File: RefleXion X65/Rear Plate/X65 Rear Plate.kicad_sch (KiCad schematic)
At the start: 4 parts

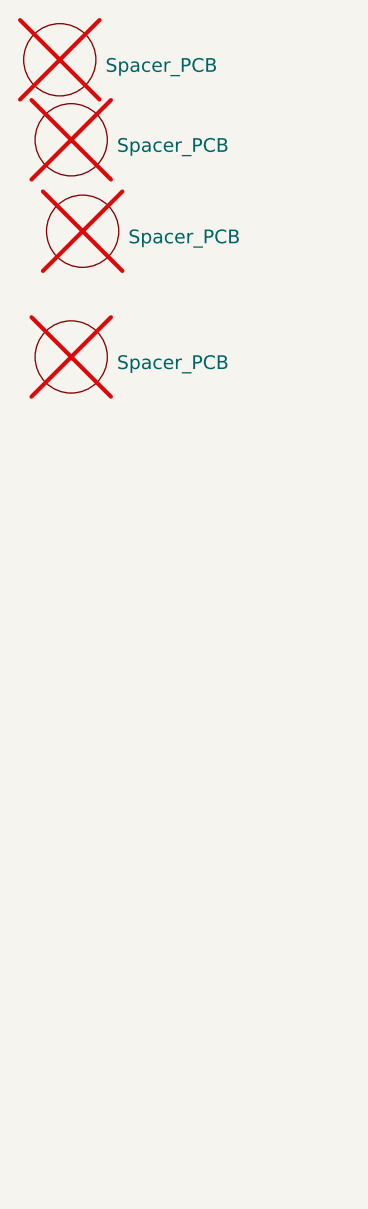
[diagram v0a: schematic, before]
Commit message: x65 Rear Plate
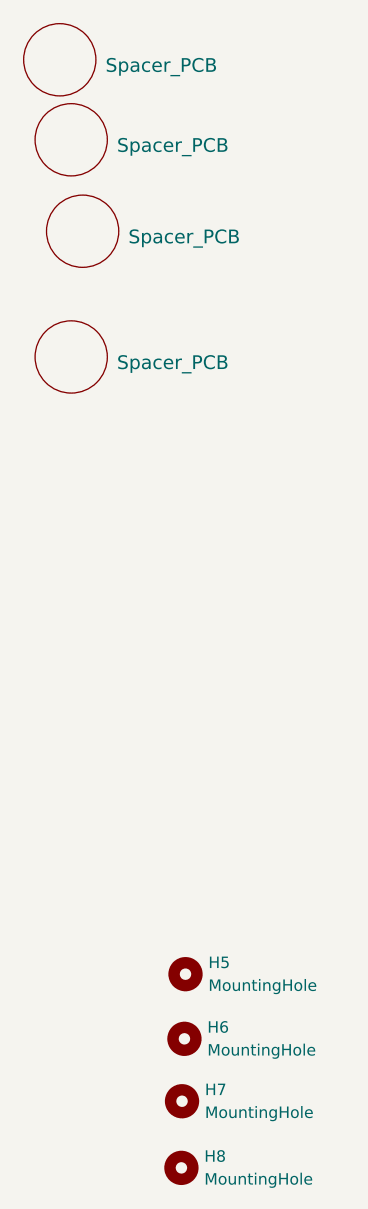
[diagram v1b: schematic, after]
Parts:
- added H5, H6, H7, H8: MountingHole, MountingHole:MountingHole_3.2mm_M3, symbol Mechanical:MountingHole
- H1, H2, H3, H4: now fitted
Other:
- title: X65 Rear -> RefleXion X65 - Blank
